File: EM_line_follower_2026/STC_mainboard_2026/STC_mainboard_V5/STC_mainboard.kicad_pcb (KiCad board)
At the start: 2 copper layers, 105 x 86.5 mm, 112 parts, among them J1 Conn_01x04, J10 Conn_01x04, J11 WirePad, J12 WirePad, J13 Conn_01x02, J14 WirePad, J15 WirePad, J16 WirePad, J2 WirePad, J20 WirePad, J21 WirePad, J23 WirePad, J24 WirePad, J3 WirePad, J4 Conn_01x04, J5 WirePad, J6 WirePad, J7 WirePad, J8 WirePad, J9 Conn_01x04, SW1 SW_Push, SW3 SW_Push, U1 STC16H40K128_CoreBoard, U10 TPS54360DDA, U3 LSM6DSRTR, U4 LM1117-3.3V, U5 OPA2197xD, U6 OPA2197xD, U7 OPA2197xD

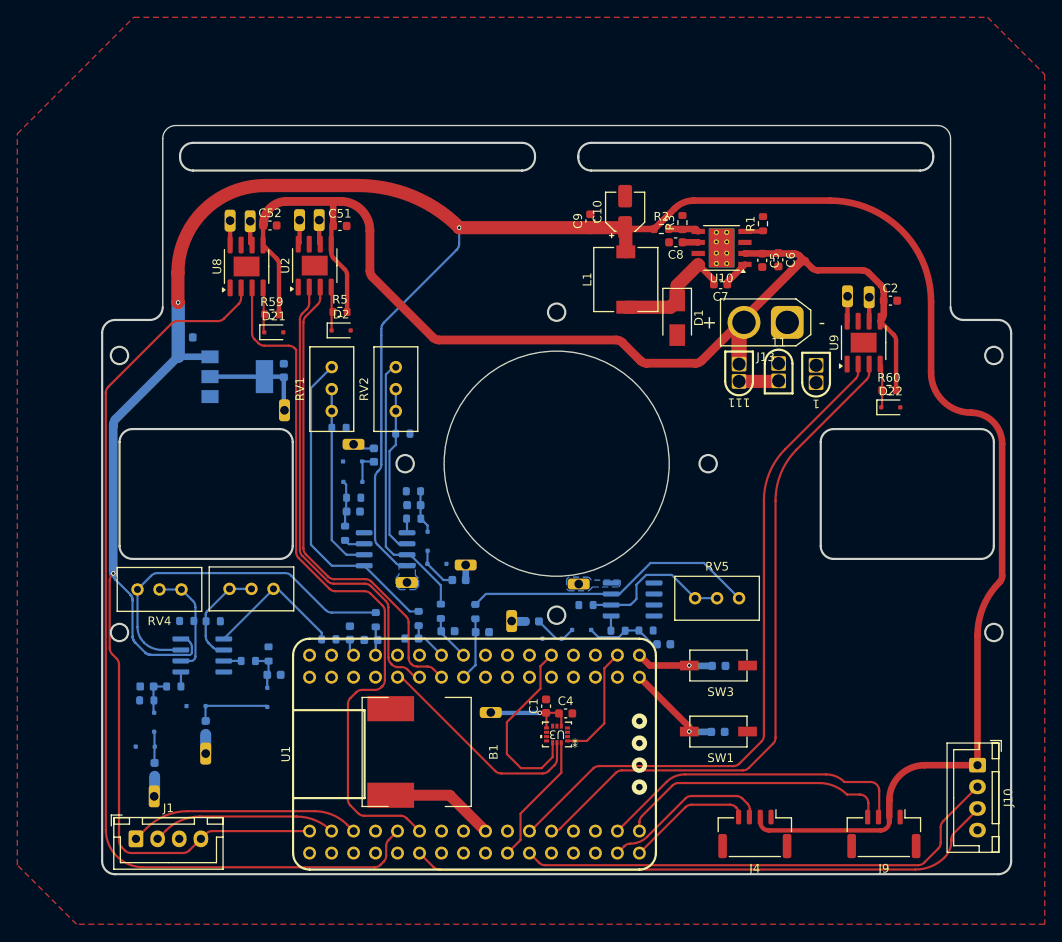
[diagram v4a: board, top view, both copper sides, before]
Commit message: change position of variable resistor
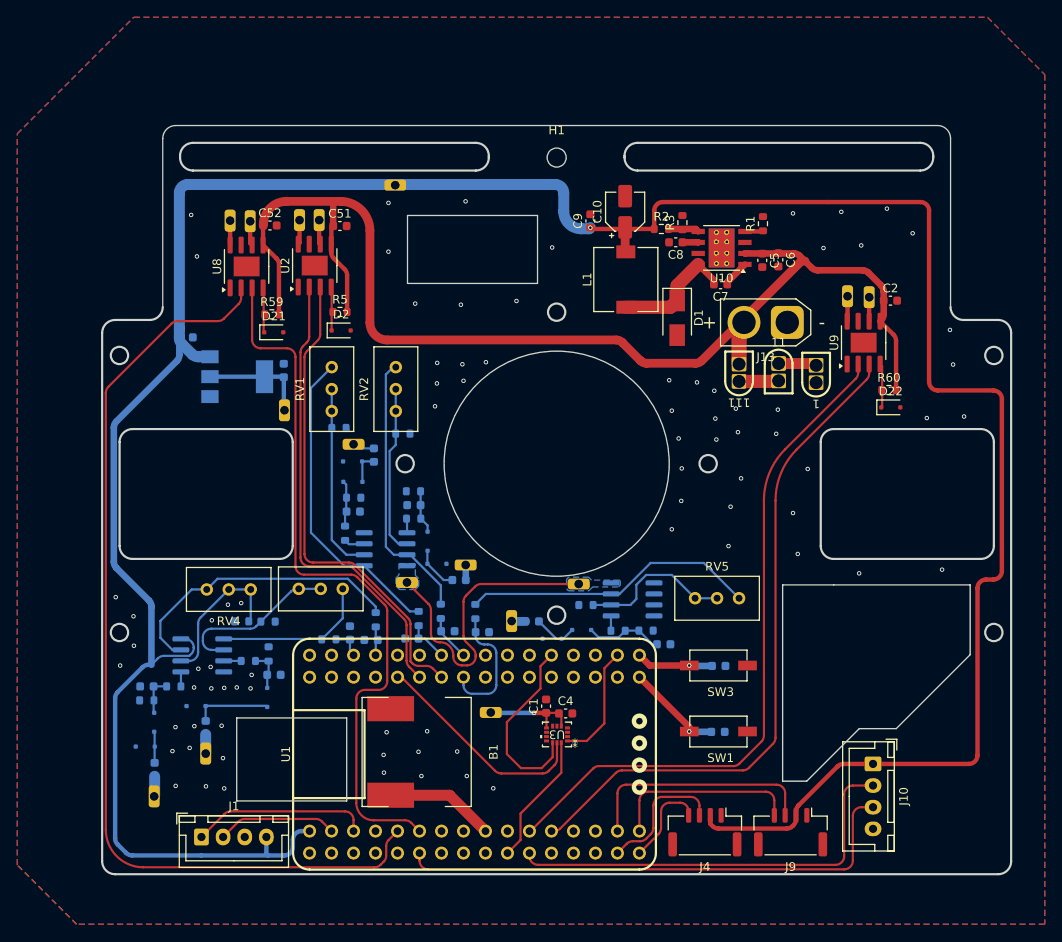
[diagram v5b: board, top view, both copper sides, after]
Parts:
- added H1: MountingHole, MountingHole:MountingHole_2.2mm_M2, F.Cu at (99.3, 123.2)
- added J15: WirePad, STC_mainboard_lib:WirePad_motor, F.Cu at (80.7, 126.5)
- moved J10 12.1 mm to (135.9, 193.3)
- moved J9 10.8 mm to (126.4, 201.2)
- moved RV4 8.00 mm to (58.9, 173.1)
- moved RV3 8.00 mm to (74.6, 173.1)
- moved J1 7.57 mm to (58.3, 201.7)
- moved R23 6.34 mm to (66.0, 176.8)
- moved R30 6.34 mm to (63.0, 176.8)
- moved J4 5.77 mm to (116.5, 201.2)
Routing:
- net /P5.0: track 32.4 -> 21.9 mm
- net +5V: track 353.5 -> 363.9 mm, vias 3 -> 1
- net /P3.4: track 37.0 -> 27.3 mm
- net /P6.3: track 68.8 -> 60.0 mm
- net /P6.5: track 57.4 -> 48.8 mm
- net /P0.1: track 7.34 -> 14.9 mm
- net /P5.2: track 21.3 -> 13.9 mm
- net Net-(U5A--): track 12.0 -> 19.4 mm
- net Net-(R25-Pad1): track 40.8 -> 33.8 mm
- net /P5.3: track 26.8 -> 20.6 mm
- net Net-(U5B--): track 12.9 -> 17.5 mm
- net /P5.1: track 15.1 -> 10.5 mm
- net Net-(1-+): track 0.00 -> 4.42 mm
- net /P3.5: track 19.9 -> 15.6 mm
- net +12V: track 139.4 -> 143.0 mm
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- added copper zone on B.Cu, net GND
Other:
- outline, holes or cut-outs redrawn
